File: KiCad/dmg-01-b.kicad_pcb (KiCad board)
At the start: 2 copper layers, 83 x 78.5 mm, 62 parts, among them CN1 SCREEN, CN2 CART, CN3 EXT, CN4 BATTERY, P1 CART SHIELD GND PADS, P2 GND PAD, P3 GND PAD, P4 GND PAD, SW1 POWER_SW, U1 CPU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

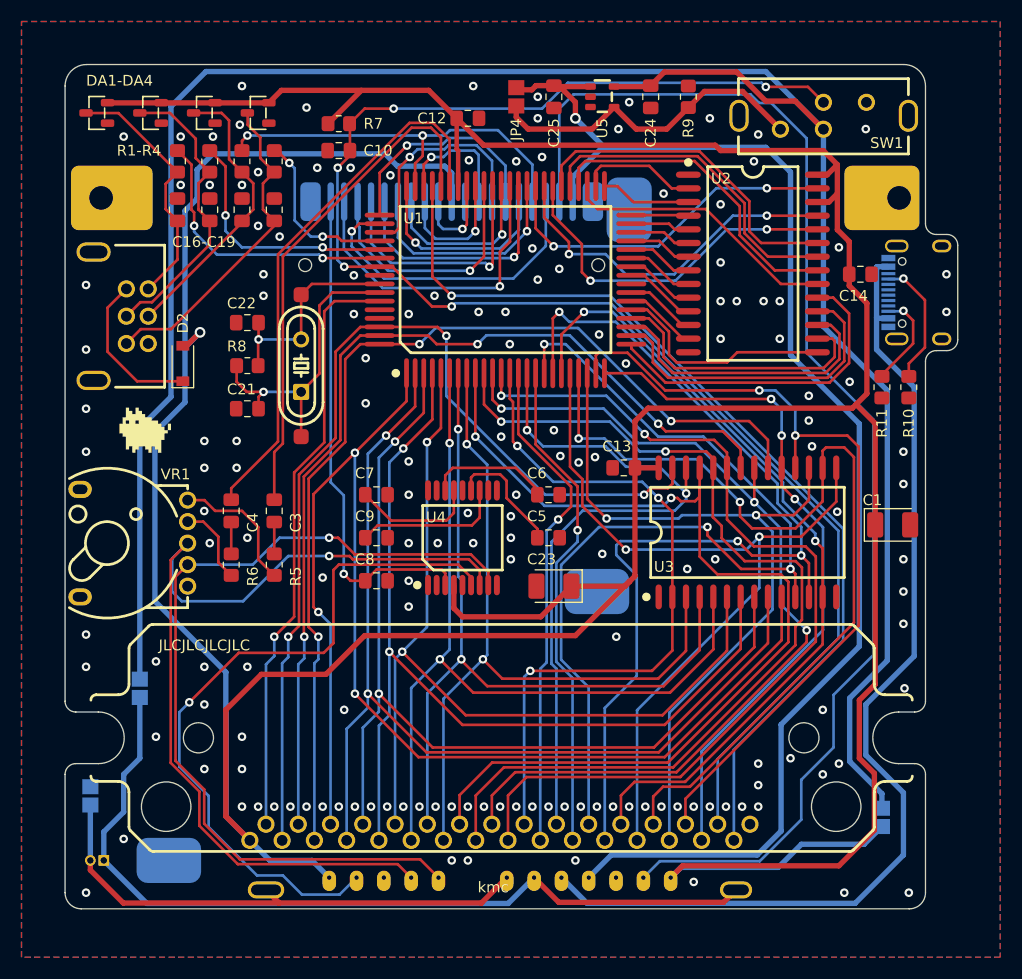
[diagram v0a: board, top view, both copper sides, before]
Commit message: significantly simplified the power stuff
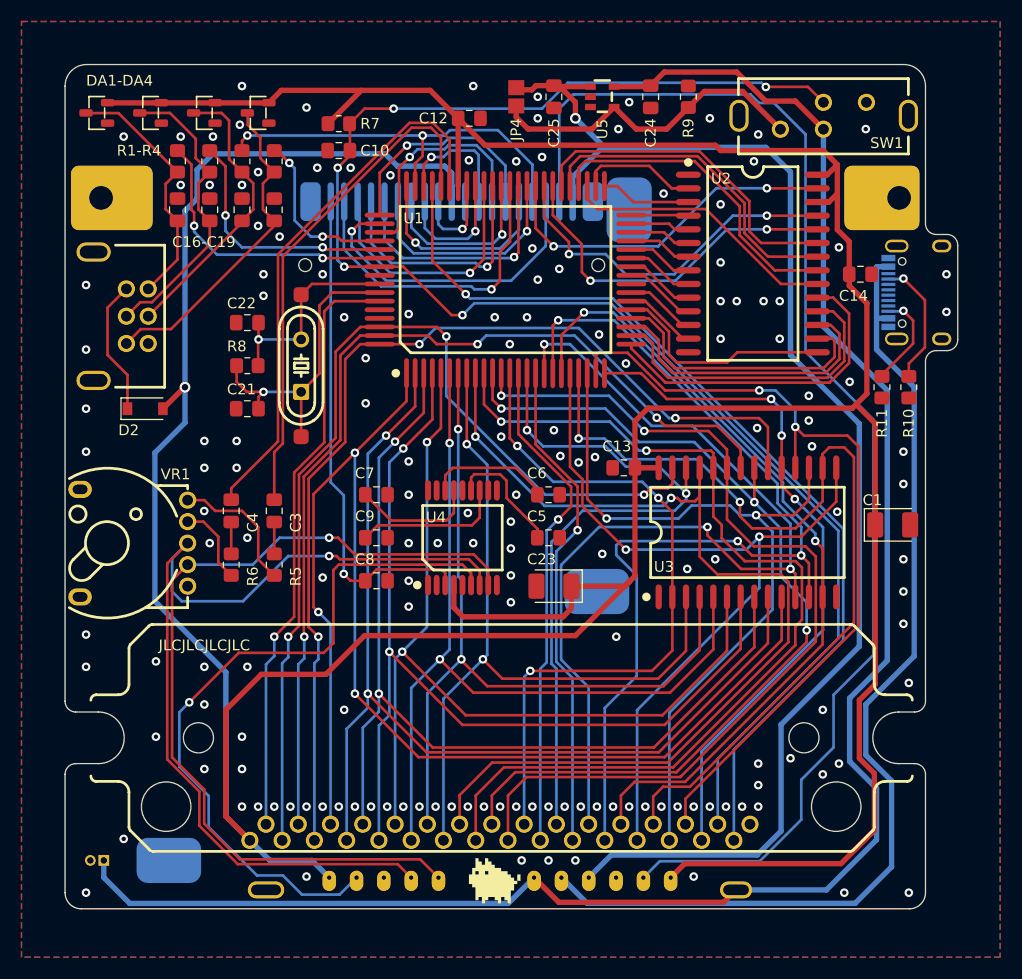
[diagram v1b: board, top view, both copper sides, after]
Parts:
- removed JP1: GND -BATT, kmc_lib:solder_jumper_x2
- removed JP2: BAT SWITCH, kmc_lib:solder_jumper_x2
- removed JP3: 5V SWITCH, kmc_lib:solder_jumper_x2
- H2: footprint kmc_lib:2.54_PAD_SMD_X7 -> kmc_lib:2.54_PAD_SMD_X6
- R9: value 1kΩ -> 10kΩ
- U5: footprint kmc_lib:SOT-23-5_L2.9-W1.6-P0.95-LS2.8-BL -> easyeda2kicad:SOT-23-5_L2.9-W1.6-P0.95-LS2.8-BL
- moved G1 53.0 mm to (70.3, 101.6)
- moved D2 5.47 mm to (37.5, 58.0), turned to 0 degrees
- moved H2 1.27 mm to (80.0, 96.5)
- moved C12 0.14 mm to (67.6, 31.0)
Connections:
- C24 pad 2: VIN -> +BATT
- CN4 pad 2: -BATT -> GND
- H1 pad 2: -BATT -> GND
- SW1 pad 1: VIN -> +BATT
- U5 pad 5: VIN -> +BATT
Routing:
- net VIN: track 209.1 -> 0.00 mm
- net +BATT: track 79.4 -> 171.9 mm
- net -BATT: track 48.8 -> 0.00 mm
- net +5V: track 416.2 -> 394.9 mm
- net Net-(CN3-Pad1): track 14.7 -> 12.6 mm
- net /D1: track 92.0 -> 90.9 mm
- net VCC: track 96.3 -> 95.4 mm
- net /SND: track 89.5 -> 88.7 mm
- net /D5: track 71.6 -> 72.4 mm
- net /CS: track 94.1 -> 94.8 mm
- net /RST: track 147.1 -> 147.7 mm
- net GND: vias 157 -> 159
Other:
- board text removed: "BAT-"
- board text removed: "kmc"

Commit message: v1.5
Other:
- board text added: "v${REVISION}"
- board text removed: "v1.4"
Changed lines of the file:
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@@
     (fp_line (start -6 5) (end -5.031 5) (layer "F.SilkS") (width 0.254))
     (fp_arc (start -2.5 4) (mid -6.581538 -0.183962) (end -6 -6) (layer "F.SilkS") (width 0.254))
-    (fp_arc (start 6 -6) (mid 6.581539 -0.183961) (end 2.5 4) (layer "F.SilkS") (width 0.254))
+    (fp_arc (start 6 -6) (mid 6.581539 -0.183962) (end 2.5 4) (layer "F.SilkS") (width 0.254))
     (fp_arc (start -3.199638 -4.100525) (mid -3.096245 -5.695327) (end -1.501 -5.599) (layer "F.SilkS") (width 0.254))
     (fp_circle (center 0 -2.5) (end 2 -2.5) (layer "F.SilkS") (width 0.254) (fill none))
@@
     (effects (font (size 1 1) (thickness 0.15)) (justify left mirror))
   )
-  (gr_text "v1.4" (at 49.5 69.2) (layer "B.SilkS")
+  (gr_text "v${REVISION}" (at 49.5 69.2) (layer "B.SilkS")
     (effects (font (size 1 1) (thickness 0.15)) (justify right mirror))
   )

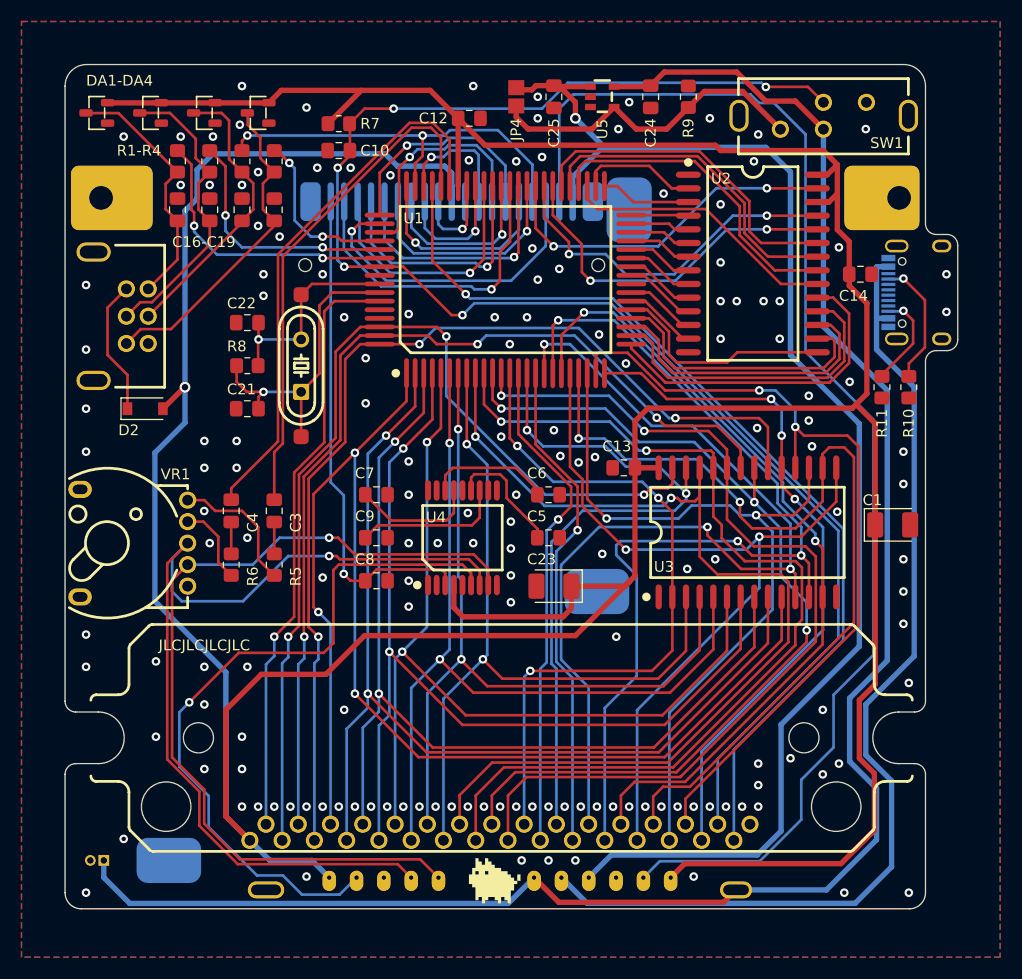
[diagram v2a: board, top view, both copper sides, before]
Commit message: minor tracks cleanup
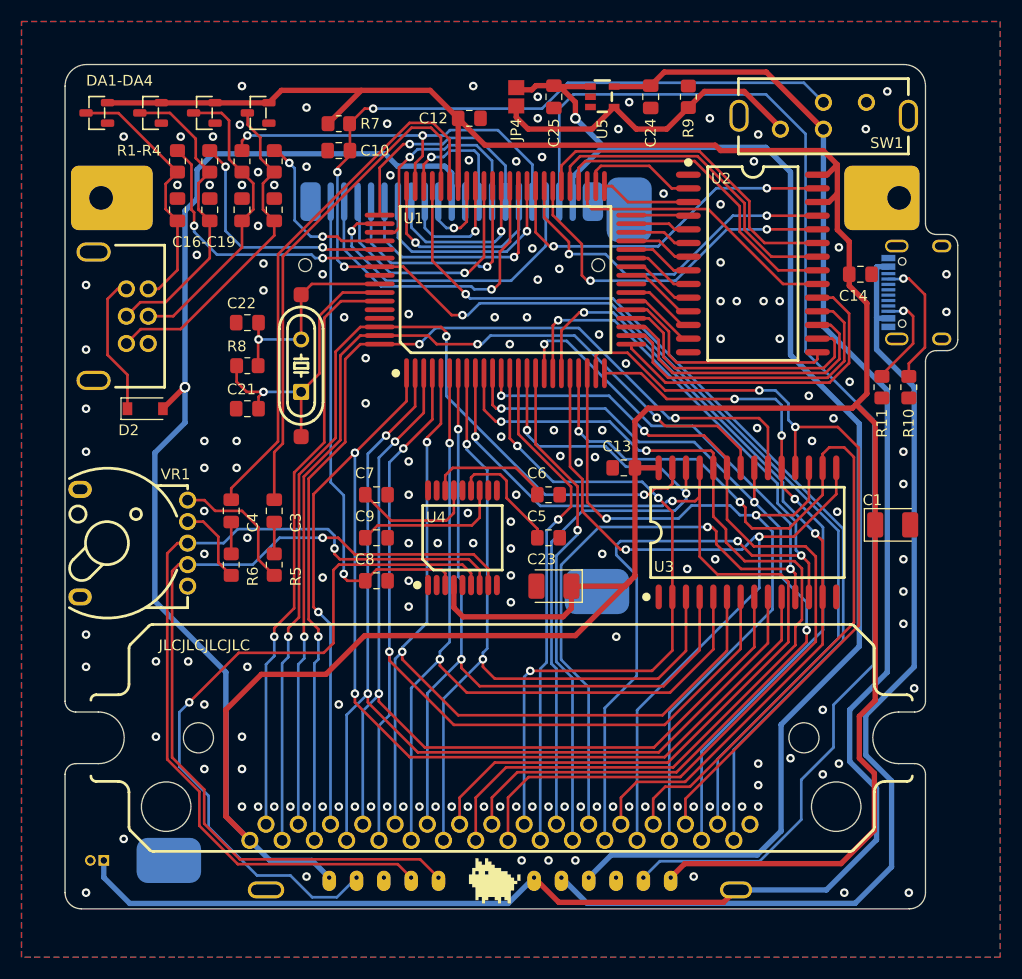
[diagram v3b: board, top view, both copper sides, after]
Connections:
- net /SWITCH renamed SW_OUT
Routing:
- net /RPOT: track 87.7 -> 82.2 mm
- net /EXT_SD: track 26.6 -> 28.0 mm
- net /D4: track 85.3 -> 84.4 mm
- net /EXT_IN: track 27.9 -> 28.7 mm
- net /A11: track 87.1 -> 86.5 mm
- net /CK1: track 28.6 -> 28.1 mm
- net /EXT_OUT: track 23.7 -> 24.2 mm
- net /EXT_CLK: track 30.2 -> 30.7 mm
- net /RST: vias 5 -> 4
- net GND: vias 159 -> 162

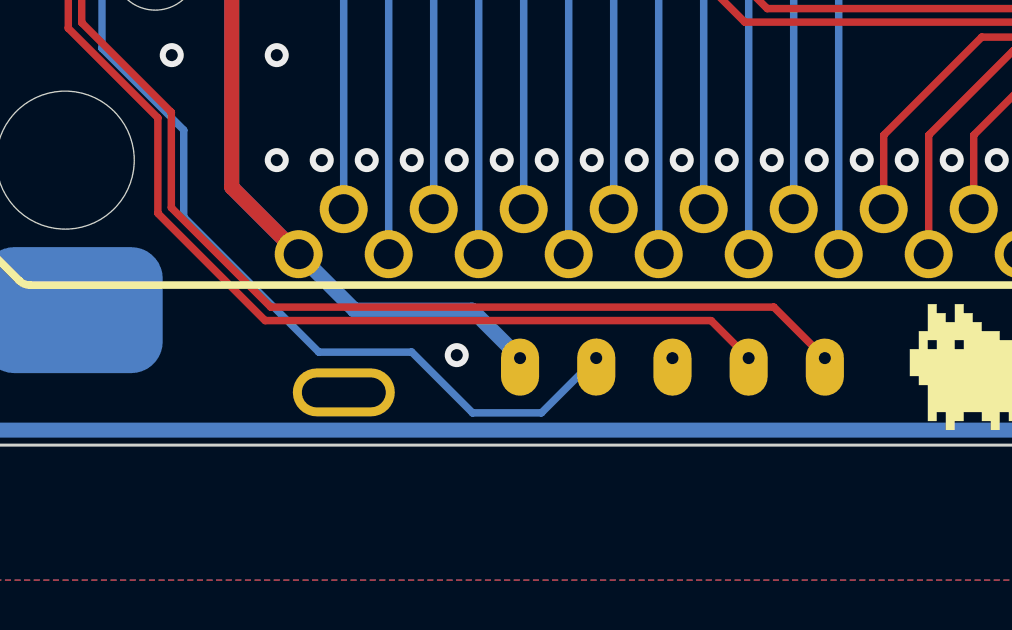
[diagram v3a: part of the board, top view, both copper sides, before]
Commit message: change side of 5v pin on the audio header
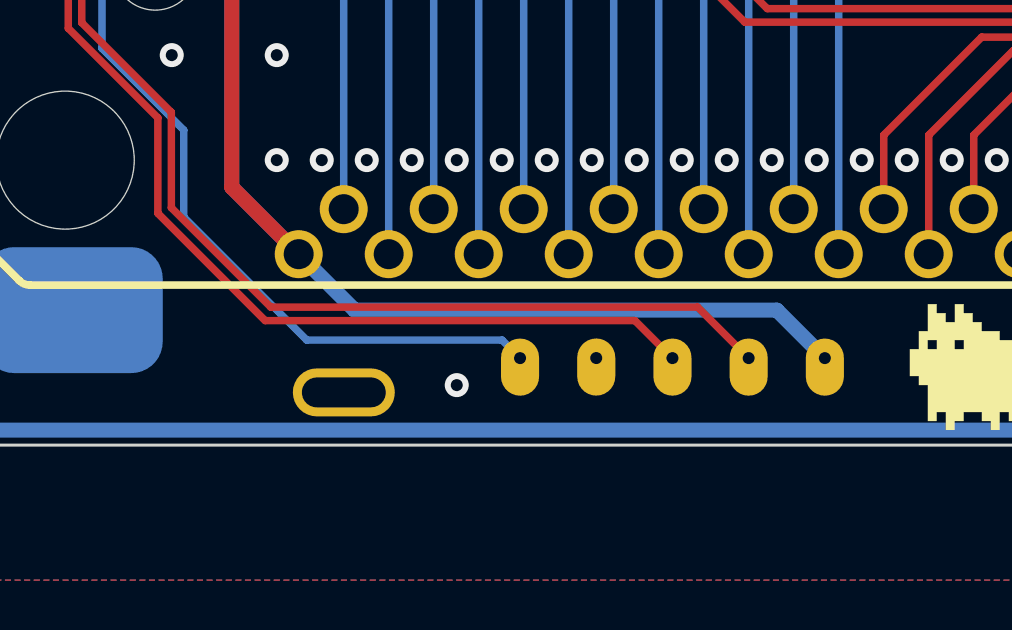
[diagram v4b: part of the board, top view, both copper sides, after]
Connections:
- H3 pad 1: /LPOT -> +5V
- H3 pad 2: /RPOT -> /LPOT
- H3 pad 3: GND -> /RPOT
- H3 pad 4: /AMP_EN -> GND
- H3 pad 5: +5V -> /AMP_EN
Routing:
- net +5V: track 394.9 -> 405.0 mm
- net /AMP_EN: track 66.5 -> 62.5 mm
- net /RPOT: track 82.2 -> 79.7 mm
- net /LPOT: track 82.0 -> 79.4 mm

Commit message: more pedantic changes
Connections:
- net +VSW renamed PD_OUT
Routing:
- net /A5: track 77.6 -> 78.5 mm
- net /D7: track 64.4 -> 63.7 mm
- net /D6: track 76.2 -> 76.8 mm

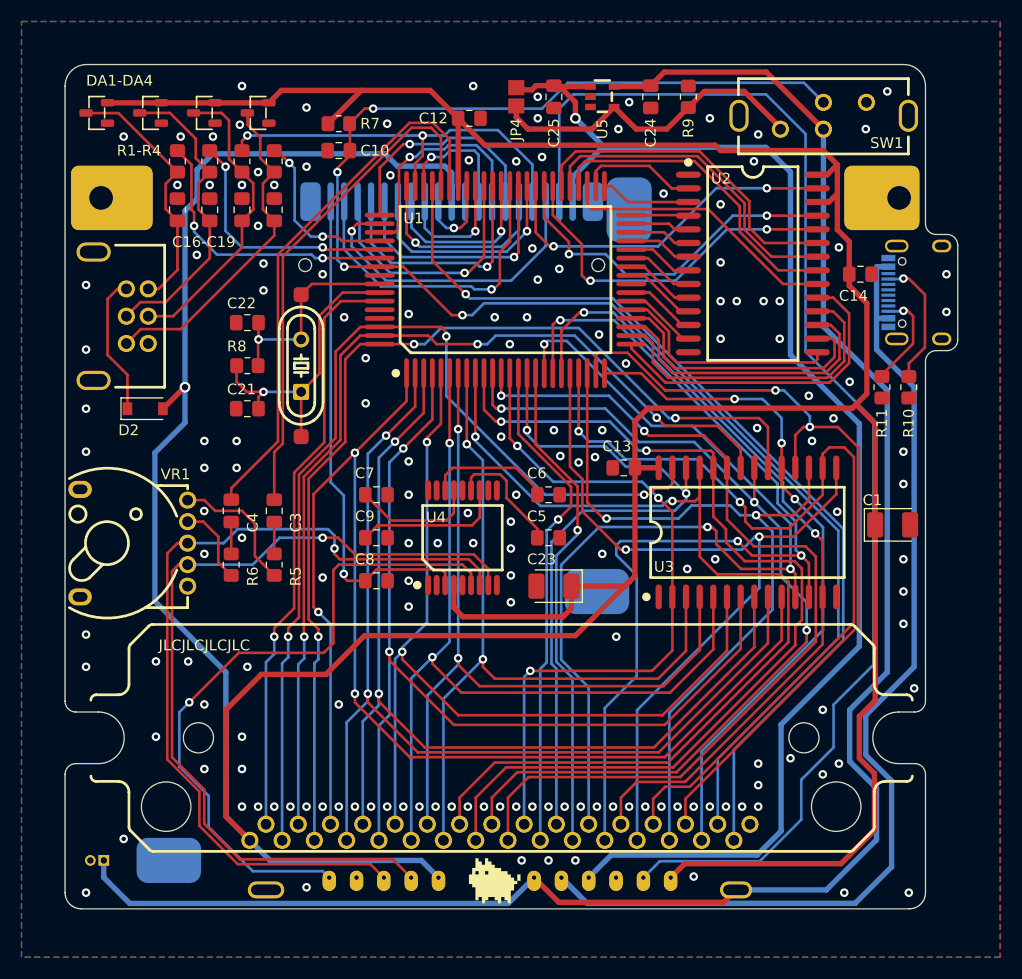
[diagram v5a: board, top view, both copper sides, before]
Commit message: better bottom pads
- more clearance between the battery terminals and bottom pads
- swapped +bat and usb on the power pads because it makes more sense
- marked more clearly where the og boards go
- small routing optimizations
- small cosmetic changes
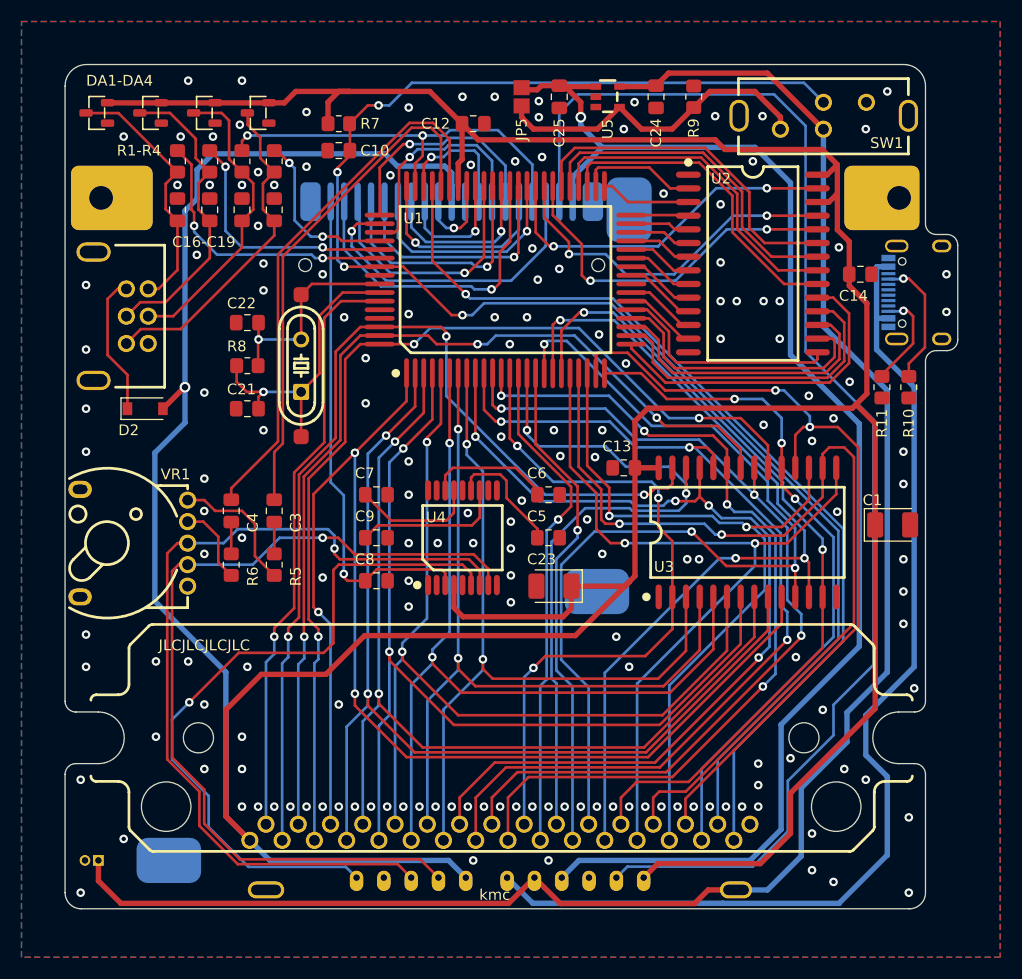
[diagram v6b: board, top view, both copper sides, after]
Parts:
- removed JP4: bypass, kmc_lib:solder_jumper_x2
- added JP5: bypass, kmc_lib:solder_jumper_x2, F.Cu at (72.5, 29.0)
- CN1: footprint dmg_lib:DMG_FPC_CONN -> kmc_lib:DMG_FPC_CONN
- G1: moved to B.Cu
- H2: footprint kmc_lib:2.54_PAD_SMD_X6 -> kmc_lib:PAD_2.54_HYBRID_X6
- H3: footprint kmc_lib:2.54_PAD_SMD_X5 -> kmc_lib:PAD_2.54_HYBRID_X5
- moved G1 36.3 mm to (69.5, 65.3), turned to 180 degrees
- moved H3 4.58 mm to (62.2, 97.8)
- moved H2 2.81 mm to (77.5, 97.8)
- moved C12 0.62 mm to (68.0, 31.5)
- moved C24 0.50 mm to (85.0, 29.0)
- moved C25 0.50 mm to (76.0, 29.0)
- moved CN4 0.50 mm to (32.5, 100.0)
- moved R9 0.50 mm to (88.5, 29.0)
- moved U5 0.50 mm to (80.5, 29.0)
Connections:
- H2 pad 5: VCC -> +BATT
- H2 pad 6: +BATT -> VCC
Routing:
- net /D1: track 91.0 -> 82.2 mm
- net +BATT: track 171.9 -> 166.8 mm
- net /MCS: track 25.0 -> 30.0 mm
- net /A8: track 92.9 -> 87.9 mm, vias 2 -> 4
- net /A11: track 86.5 -> 81.6 mm, vias 2 -> 4
- net VCC: track 95.4 -> 99.2 mm
- net /D4: track 84.4 -> 88.0 mm
- net /AMP_EN: track 62.5 -> 65.6 mm
- net VEE: track 119.7 -> 122.3 mm
- net /RPOT: track 79.7 -> 82.2 mm
- net /LPOT: track 79.4 -> 82.0 mm
- net PD_OUT: track 125.7 -> 127.3 mm
- net /D5: track 72.5 -> 71.0 mm
- net /A9: track 89.3 -> 87.8 mm, vias 2 -> 3
- net /A10: track 87.0 -> 85.7 mm
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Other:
- board text added: "CONV"
- board text added: "JACK"
- board text added: "kmc"
- board text removed: "+"
- board text removed: "-"
